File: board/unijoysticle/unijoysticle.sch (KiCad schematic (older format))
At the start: 14 parts, among them IC1 74LS05, IC2 74LS05, J1 DB9_Female, J2 DB9_Female, J3 Barrel_Jack, SW1 SW_Push, SW2 SW_SPST

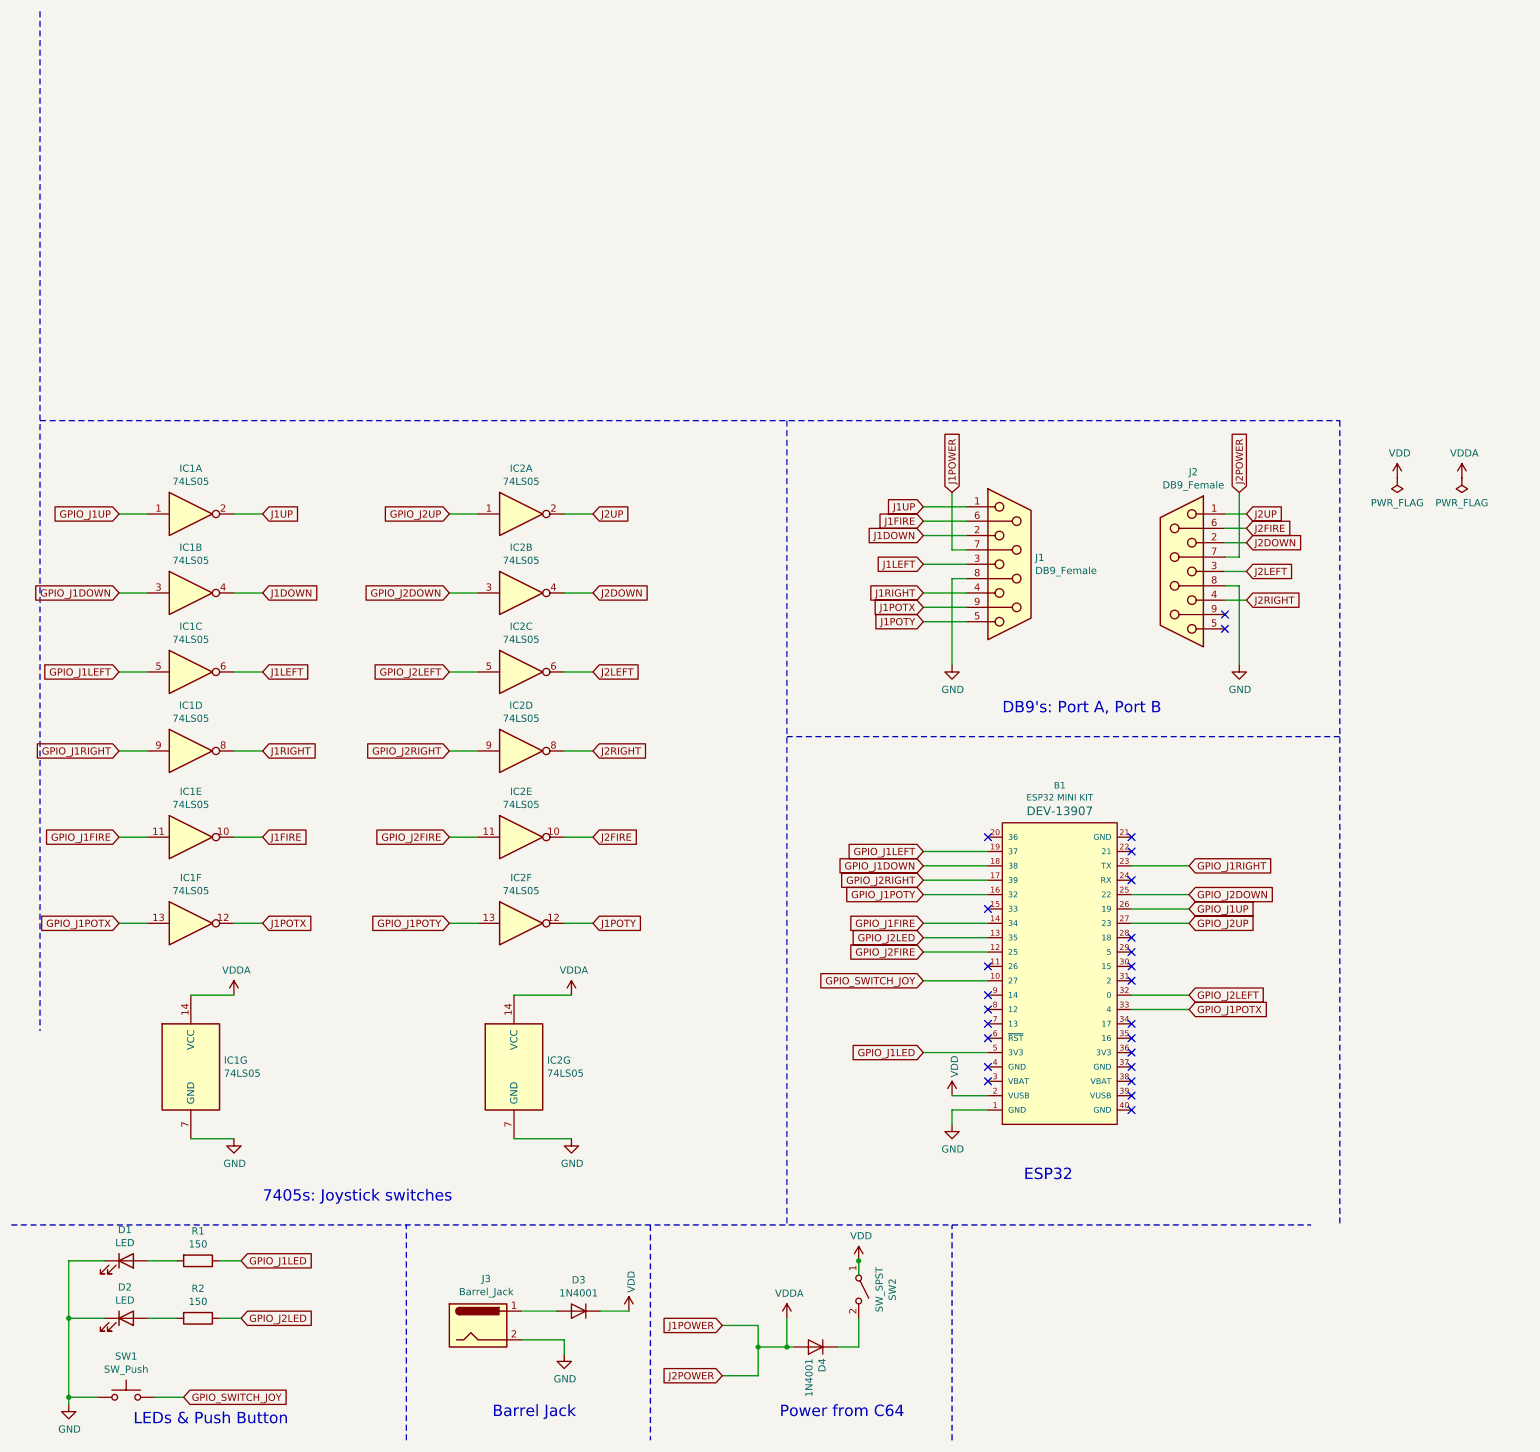
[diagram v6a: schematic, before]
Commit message: board: Rev F
* Use Schottky diodes
* Add mounting hole
* Logo is "locked"
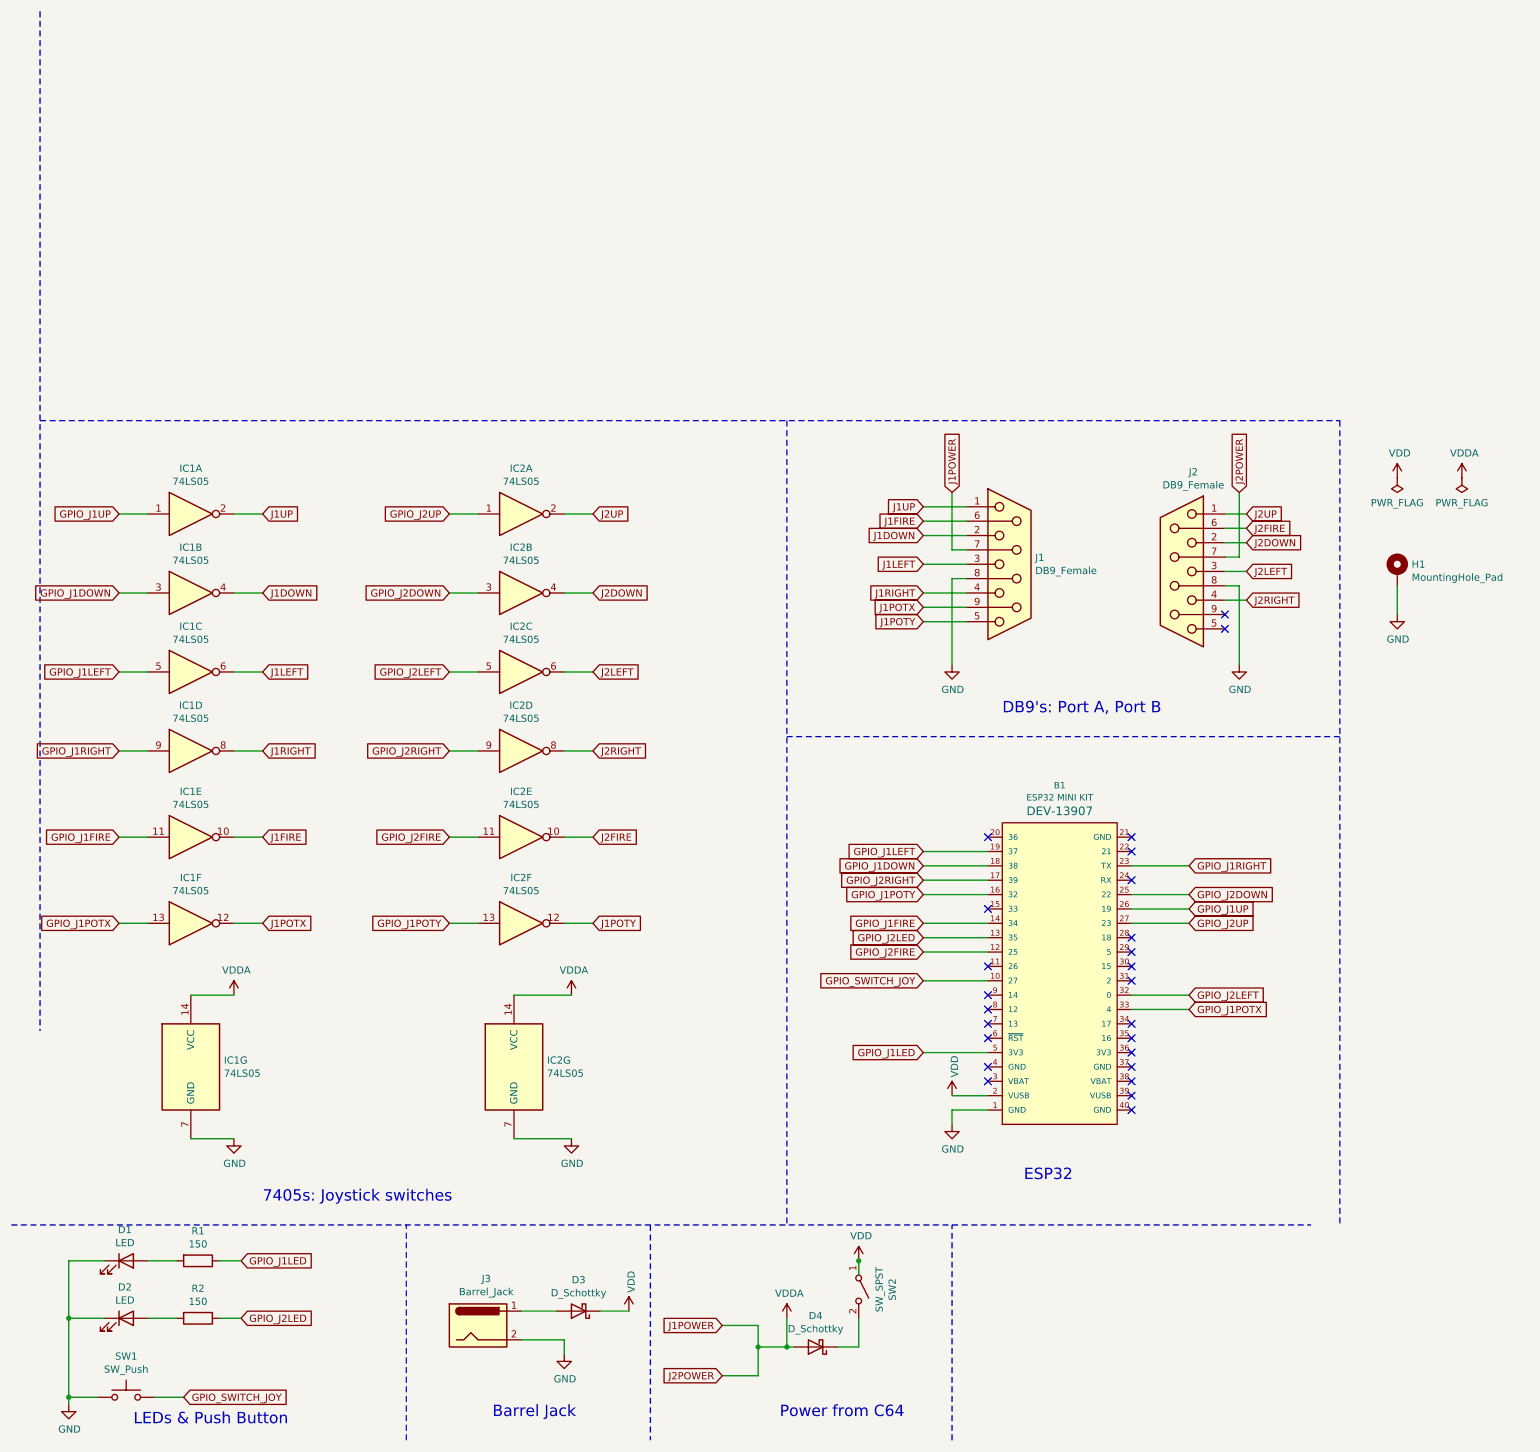
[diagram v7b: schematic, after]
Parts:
- removed D3, D4: 1N4001, Diode_THT:D_DO-41_SOD81_P7.62mm_Horizontal, symbol Diode:1N4001
- added D3, D4: D_Schottky, Diode_THT:D_DO-35_SOD27_P7.62mm_Horizontal, symbol Device:D_Schottky
- added H1: MountingHole_Pad, MountingHole:MountingHole_2.2mm_M2_Pad, symbol Mechanical:MountingHole_Pad
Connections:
- net GND: now also H1.1
- net VDD: now also D3.1 (K)
- net VDDA: now also D4.2 (A)
- net at J3.1: now also D3.2 (A)
- net at SW2.2 (B): now also D4.1 (K)
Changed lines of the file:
@@
 EESchema Schematic File Version 4
-LIBS:unijoysticle-cache
 EELAYER 30 0
 EELAYER END
@@
 Title "Unijoysticle 2"
 Date "2019-09-27"
-Rev "D"
+Rev "F"
 Comp "Retro Moe"
 Comment1 "Ricardo Quesada"
@@
 $EndComp
 $Comp
-L Diode:1N4001 D3
-U 1 1 5CA00191
-P 4300 6900
-F 0 "D3" H 4300 6684 50  0000 C CNN
-F 1 "1N4001" H 4300 6775 50  0000 C CNN
-F 2 "Diode_THT:D_DO-41_SOD81_P7.62mm_Horizontal" H 4300 6725 50  0001 C CNN
-F 3 "http://www.vishay.com/docs/88503/1n4001.pdf" H 4300 6900 50  0001 C CNN
-	1    4300 6900
-	-1   0    0    1
-$EndComp
-$Comp
 L Connector:Barrel_Jack J3
 U 1 1 5CA09684
@@
 Wire Wire Line
 	5550 7150 5550 7350
-$Comp
-L Diode:1N4001 D4
-U 1 1 5DA3B4FA
-P 5950 7150
-F 0 "D4" V 5904 7229 50  0000 L CNN
-F 1 "1N4001" V 5995 7229 50  0000 L CNN
-F 2 "Diode_THT:D_DO-41_SOD81_P7.62mm_Horizontal" H 5950 6975 50  0001 C CNN
-F 3 "http://www.vishay.com/docs/88503/1n4001.pdf" H 5950 7150 50  0001 C CNN
-	1    5950 7150
-	-1   0    0    1
-$EndComp
 Wire Wire Line
 	6250 6650 6250 6550
@@
 	-1   0    0    1
 $EndComp
+$Comp
+L Device:D_Schottky D3
+U 1 1 5F66A0AA
+P 4300 6900
+F 0 "D3" H 4300 6683 50  0000 C CNN
+F 1 "D_Schottky" H 4300 6774 50  0000 C CNN
+F 2 "Diode_THT:D_DO-35_SOD27_P7.62mm_Horizontal" H 4300 6900 50  0001 C CNN
+F 3 "~" H 4300 6900 50  0001 C CNN
+	1    4300 6900
+	-1   0    0    1
+$EndComp
+$Comp
+L Device:D_Schottky D4
+U 1 1 5F66BD2F
+P 5950 7150
+F 0 "D4" H 5950 6933 50  0000 C CNN
+F 1 "D_Schottky" H 5950 7024 50  0000 C CNN
+F 2 "Diode_THT:D_DO-35_SOD27_P7.62mm_Horizontal" H 5950 7150 50  0001 C CNN
+F 3 "~" H 5950 7150 50  0001 C CNN
+	1    5950 7150
+	-1   0    0    1
+$EndComp
+$Comp
+L Mechanical:MountingHole_Pad H1
+U 1 1 5F6B0E64
+P 10000 1750
+F 0 "H1" H 10100 1799 50  0000 L CNN
+F 1 "MountingHole_Pad" H 10100 1708 50  0000 L CNN
+F 2 "MountingHole:MountingHole_2.2mm_M2_Pad" H 10000 1750 50  0001 C CNN
+F 3 "~" H 10000 1750 50  0001 C CNN
+	1    10000 1750
+	1    0    0    -1
+$EndComp
+$Comp
+L power:GND #PWR0116
+U 1 1 5F6BE84B
+P 10000 2050
+F 0 "#PWR0116" H 10000 1800 50  0001 C CNN
+F 1 "GND" H 10005 1877 50  0000 C CNN
+F 2 "" H 10000 2050 50  0001 C CNN
+F 3 "" H 10000 2050 50  0001 C CNN
+	1    10000 2050
+	1    0    0    -1
+$EndComp
+Wire Wire Line
+	10000 1850 10000 2050
 $EndSCHEMATC

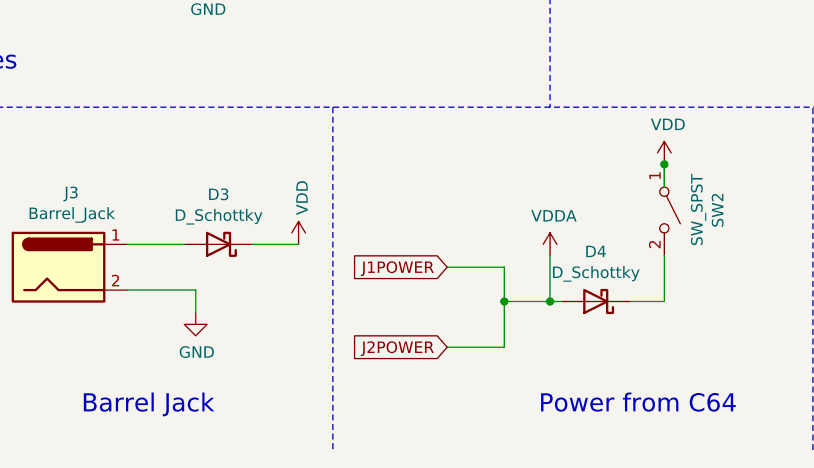
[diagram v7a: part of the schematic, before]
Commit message: board: uses 1n5819 (schottky) instead of just a bare "schotkky"
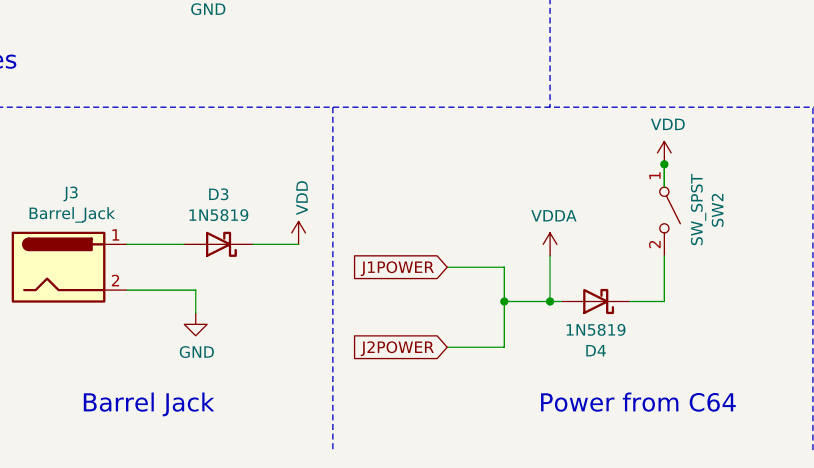
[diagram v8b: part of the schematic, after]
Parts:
- removed D3, D4: D_Schottky, Diode_THT:D_DO-35_SOD27_P7.62mm_Horizontal, symbol Device:D_Schottky
- added D3, D4: 1N5819, Diode_THT:D_DO-41_SOD81_P7.62mm_Horizontal, symbol Diode:1N5819
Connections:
- net VDD: now also D3.1 (K)
- net VDDA: now also D4.2 (A)
- net at J3.1: now also D3.2 (A)
- net at SW2.2 (B): now also D4.1 (K)
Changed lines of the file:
@@
-$EndComp
-$Comp
-L Device:D_Schottky D3
-U 1 1 5F66A0AA
-P 4300 6900
-F 0 "D3" H 4300 6683 50  0000 C CNN
-F 1 "D_Schottky" H 4300 6774 50  0000 C CNN
-F 2 "Diode_THT:D_DO-35_SOD27_P7.62mm_Horizontal" H 4300 6900 50  0001 C CNN
-F 3 "~" H 4300 6900 50  0001 C CNN
-	1    4300 6900
-	-1   0    0    1
-$EndComp
-$Comp
-L Device:D_Schottky D4
-U 1 1 5F66BD2F
-P 5950 7150
-F 0 "D4" H 5950 6933 50  0000 C CNN
-F 1 "D_Schottky" H 5950 7024 50  0000 C CNN
-F 2 "Diode_THT:D_DO-35_SOD27_P7.62mm_Horizontal" H 5950 7150 50  0001 C CNN
-F 3 "~" H 5950 7150 50  0001 C CNN
-	1    5950 7150
-	-1   0    0    1
 $EndComp
 $Comp
@@
 Wire Wire Line
 	10000 1850 10000 2050
+$Comp
+L Diode:1N5819 D3
+U 1 1 5F697863
+P 4300 6900
+F 0 "D3" H 4300 6683 50  0000 C CNN
+F 1 "1N5819" H 4300 6774 50  0000 C CNN
+F 2 "Diode_THT:D_DO-41_SOD81_P7.62mm_Horizontal" H 4300 6725 50  0001 C CNN
+F 3 "http://www.vishay.com/docs/88525/1n5817.pdf" H 4300 6900 50  0001 C CNN
+	1    4300 6900
+	-1   0    0    1
+$EndComp
+$Comp
+L Diode:1N5819 D4
+U 1 1 5F695DDA
+P 5950 7150
+F 0 "D4" H 5950 7367 50  0000 C CNN
+F 1 "1N5819" H 5950 7276 50  0000 C CNN
+F 2 "Diode_THT:D_DO-41_SOD81_P7.62mm_Horizontal" H 5950 6975 50  0001 C CNN
+F 3 "http://www.vishay.com/docs/88525/1n5817.pdf" H 5950 7150 50  0001 C CNN
+	1    5950 7150
+	-1   0    0    1
+$EndComp
 $EndSCHEMATC
